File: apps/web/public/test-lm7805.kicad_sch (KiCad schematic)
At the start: 5 parts, among them J1 VIN_CONN, J2 VOUT_5V, U1 LM7805

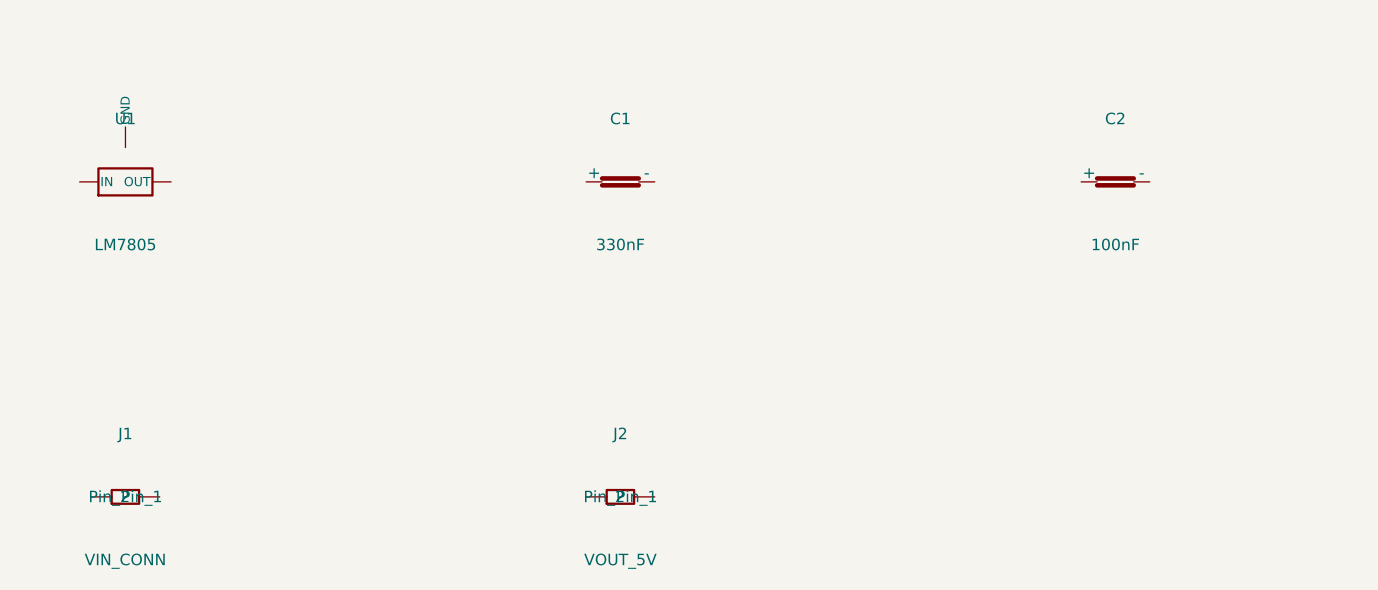
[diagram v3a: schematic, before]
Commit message: fix(schematic): add 20mm side margin to clear inner frame border
Components U1/J1 (left column) and far-right components were drawn
on top of the KiCad inner frame vertical borders (at x=10mm from
paper edge). The previous 12mm margin_side only gave 2mm clearance.

Changes:
- margin_side 12 -> 20mm in _build_flat_schematic_with_net_labels()
  (gives 10mm clearance from inner frame on both sides)
- Regenerated test-lm7805 / test-ne555 / test-esp32 .kicad_sch via
  /circuit-synth/generate (paper width 149 -> 165mm as a result)
- test-cs.html: ResizeObserver on canvas + window load/resize retries
  to reapply auto-zoom when KiCanvas resets its camera on layout
  changes (fixes title block peeking before click-to-interact)

Verified via Chrome DevTools screenshots on all 3 schematic tabs.
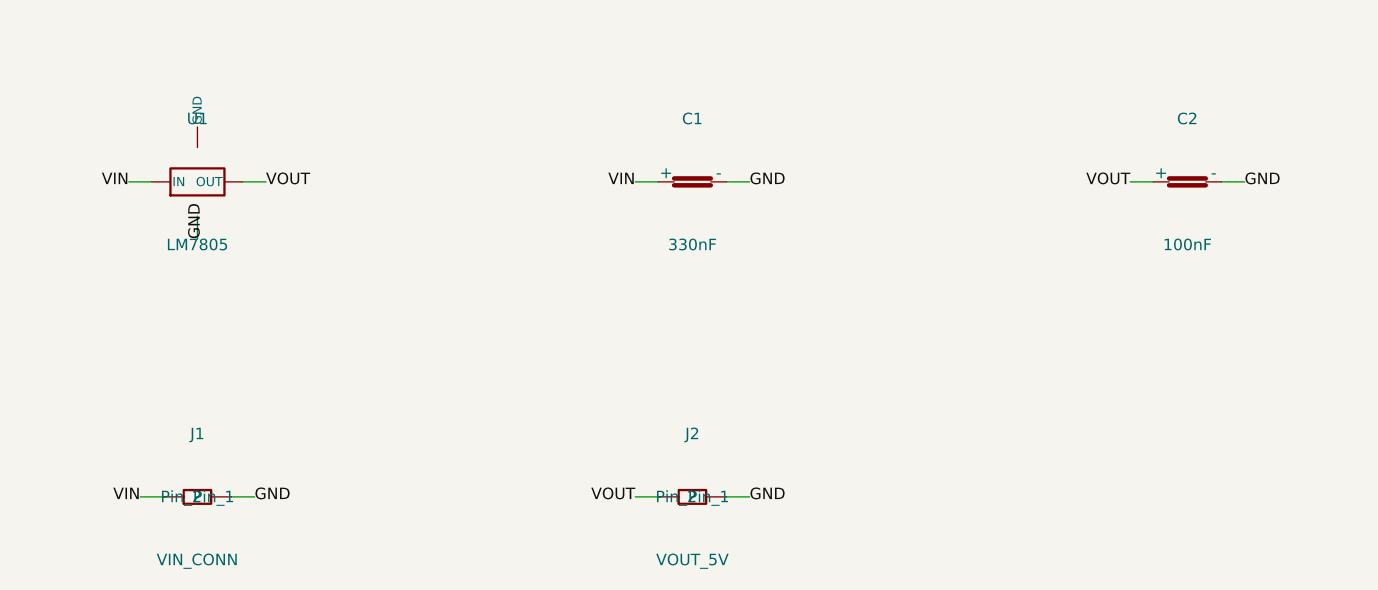
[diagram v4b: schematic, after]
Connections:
- net VIN: now reaches J1.1 (Pin_1)
- net VIN: now also C1.1 (+), U1.1 (IN)
- net GND: now reaches J1.2 (Pin_2)
- net GND: now also C1.2 (-), C2.2 (-), J2.2 (Pin_2)
- net VOUT: now reaches J2.1 (Pin_1)
- net VOUT: now also C2.1 (+), U1.3 (OUT)
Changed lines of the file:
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@@
 (kicad_sch (version 20230121) (generator "layrix-circuit-synth")
-  (paper "User" 149 123)
-  (symbol (lib_id "Device:VReg_3Pin") (at 12 20 0) (unit 1) (in_bom yes) (on_board yes)
-    (property "Reference" "U1" (at 12 13 0) (effects (font (size 1.27 1.27)) (justify center)))
-    (property "Value" "LM7805" (at 12 27 0) (effects (font (size 1.27 1.27)) (justify center)))
-    (property "Footprint" "Package_TO_SOT_THT:TO-220-3_Vertical" (at 12 30 0) (effects (font (size 1.27 1.27)) (hide yes)))
+  (paper "User" 165 123)
+  (symbol (lib_id "Device:VReg_3Pin") (at 20 20 0) (unit 1) (in_bom yes) (on_board yes)
+    (property "Reference" "U1" (at 20 13 0) (effects (font (size 1.27 1.27)) (justify center)))
+    (property "Value" "LM7805" (at 20 27 0) (effects (font (size 1.27 1.27)) (justify center)))
+    (property "Footprint" "Package_TO_SOT_THT:TO-220-3_Vertical" (at 20 30 0) (effects (font (size 1.27 1.27)) (hide yes)))
   )
-  (symbol (lib_id "Device:C") (at 67 20 0) (unit 1) (in_bom yes) (on_board yes)
-    (property "Reference" "C1" (at 67 13 0) (effects (font (size 1.27 1.27)) (justify center)))
-    (property "Value" "330nF" (at 67 27 0) (effects (font (size 1.27 1.27)) (justify center)))
-    (property "Footprint" "Capacitor_THT:C_Disc_D5.0mm_W2.5mm_P5.00mm" (at 67 30 0) (effects (font (size 1.27 1.27)) (hide yes)))
+  (symbol (lib_id "Device:C") (at 75 20 0) (unit 1) (in_bom yes) (on_board yes)
+    (property "Reference" "C1" (at 75 13 0) (effects (font (size 1.27 1.27)) (justify center)))
+    (property "Value" "330nF" (at 75 27 0) (effects (font (size 1.27 1.27)) (justify center)))
+    (property "Footprint" "Capacitor_THT:C_Disc_D5.0mm_W2.5mm_P5.00mm" (at 75 30 0) (effects (font (size 1.27 1.27)) (hide yes)))
   )
-  (symbol (lib_id "Device:C") (at 122 20 0) (unit 1) (in_bom yes) (on_board yes)
-    (property "Reference" "C2" (at 122 13 0) (effects (font (size 1.27 1.27)) (justify center)))
-    (property "Value" "100nF" (at 122 27 0) (effects (font (size 1.27 1.27)) (justify center)))
-    (property "Footprint" "Capacitor_THT:C_Disc_D5.0mm_W2.5mm_P5.00mm" (at 122 30 0) (effects (font (size 1.27 1.27)) (hide yes)))
+  (symbol (lib_id "Device:C") (at 130 20 0) (unit 1) (in_bom yes) (on_board yes)
+    (property "Reference" "C2" (at 130 13 0) (effects (font (size 1.27 1.27)) (justify center)))
+    (property "Value" "100nF" (at 130 27 0) (effects (font (size 1.27 1.27)) (justify center)))
+    (property "Footprint" "Capacitor_THT:C_Disc_D5.0mm_W2.5mm_P5.00mm" (at 130 30 0) (effects (font (size 1.27 1.27)) (hide yes)))
   )
-  (symbol (lib_id "Connector_Generic:Conn_01x02") (at 12 55 0) (unit 1) (in_bom yes) (on_board yes)
-    (property "Reference" "J1" (at 12 48 0) (effects (font (size 1.27 1.27)) (justify center)))
-    (property "Value" "VIN_CONN" (at 12 62 0) (effects (font (size 1.27 1.27)) (justify center)))
-    (property "Footprint" "Connector_PinHeader_2.54mm:PinHeader_1x02_P2.54mm_Vertical" (at 12 65 0) (effects (font (size 1.27 1.27)) (hide yes)))
+  (symbol (lib_id "Connector_Generic:Conn_01x02") (at 20 55 0) (unit 1) (in_bom yes) (on_board yes)
+    (property "Reference" "J1" (at 20 48 0) (effects (font (size 1.27 1.27)) (justify center)))
+    (property "Value" "VIN_CONN" (at 20 62 0) (effects (font (size 1.27 1.27)) (justify center)))
+    (property "Footprint" "Connector_PinHeader_2.54mm:PinHeader_1x02_P2.54mm_Vertical" (at 20 65 0) (effects (font (size 1.27 1.27)) (hide yes)))
   )
-  (symbol (lib_id "Connector_Generic:Conn_01x02") (at 67 55 0) (unit 1) (in_bom yes) (on_board yes)
-    (property "Reference" "J2" (at 67 48 0) (effects (font (size 1.27 1.27)) (justify center)))
-    (property "Value" "VOUT_5V" (at 67 62 0) (effects (font (size 1.27 1.27)) (justify center)))
-    (property "Footprint" "Connector_PinHeader_2.54mm:PinHeader_1x02_P2.54mm_Vertical" (at 67 65 0) (effects (font (size 1.27 1.27)) (hide yes)))
+  (symbol (lib_id "Connector_Generic:Conn_01x02") (at 75 55 0) (unit 1) (in_bom yes) (on_board yes)
+    (property "Reference" "J2" (at 75 48 0) (effects (font (size 1.27 1.27)) (justify center)))
+    (property "Value" "VOUT_5V" (at 75 62 0) (effects (font (size 1.27 1.27)) (justify center)))
+    (property "Footprint" "Connector_PinHeader_2.54mm:PinHeader_1x02_P2.54mm_Vertical" (at 75 65 0) (effects (font (size 1.27 1.27)) (hide yes)))
   )
+  (wire (pts (xy 14.92 20.0) (xy 12.38 20.0)) (stroke (width 0.1524) (type default)))
+  (label "VIN" (at 12.38 20.0 180) (effects (font (size 1.27 1.27))))
+  (wire (pts (xy 71.19 20.0) (xy 68.65 20.0)) (stroke (width 0.1524) (type default)))
+  (label "VIN" (at 68.65 20.0 180) (effects (font (size 1.27 1.27))))
+  (wire (pts (xy 16.19 55.0) (xy 13.65 55.0)) (stroke (width 0.1524) (type default)))
+  (label "VIN" (at 13.65 55.0 180) (effects (font (size 1.27 1.27))))
+  (wire (pts (xy 20.0 23.81) (xy 20.0 26.35)) (stroke (width 0.1524) (type default)))
+  (label "GND" (at 20.0 26.35 90) (effects (font (size 1.27 1.27))))
+  (wire (pts (xy 78.81 20.0) (xy 81.35 20.0)) (stroke (width 0.1524) (type default)))
+  (label "GND" (at 81.35 20.0 0) (effects (font (size 1.27 1.27))))
+  (wire (pts (xy 133.81 20.0) (xy 136.35 20.0)) (stroke (width 0.1524) (type default)))
+  (label "GND" (at 136.35 20.0 0) (effects (font (size 1.27 1.27))))
+  (wire (pts (xy 23.81 55.0) (xy 26.35 55.0)) (stroke (width 0.1524) (type default)))
+  (label "GND" (at 26.35 55.0 0) (effects (font (size 1.27 1.27))))
+  (wire (pts (xy 78.81 55.0) (xy 81.35 55.0)) (stroke (width 0.1524) (type default)))
+  (label "GND" (at 81.35 55.0 0) (effects (font (size 1.27 1.27))))
+  (wire (pts (xy 25.08 20.0) (xy 27.62 20.0)) (stroke (width 0.1524) (type default)))
+  (label "VOUT" (at 27.62 20.0 0) (effects (font (size 1.27 1.27))))
+  (wire (pts (xy 126.19 20.0) (xy 123.65 20.0)) (stroke (width 0.1524) (type default)))
+  (label "VOUT" (at 123.65 20.0 180) (effects (font (size 1.27 1.27))))
+  (wire (pts (xy 71.19 55.0) (xy 68.65 55.0)) (stroke (width 0.1524) (type default)))
+  (label "VOUT" (at 68.65 55.0 180) (effects (font (size 1.27 1.27))))
   (sheet_instances (path "/" (page "1")))
 )

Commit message: fix(schematic): bump margin_side to 28mm so net-label text stays inside frame
Previous 20mm margin put component body 10mm inside the inner frame,
but net-label text ("VIN", "VOUT", "GND"...) extends ~8mm left/right
of the body — so label text sat only ~3mm from the inner frame border,
looking cramped.

New 28mm margin_side accounts for the 8mm label overhang:
  component body at x=28mm
  label text reaches x=28-8=20mm
  inner frame at x=10mm
  -> 10mm visual clearance between label text and frame border

Paper width grows 165 -> 181mm. Regenerated all 3 test schematics.
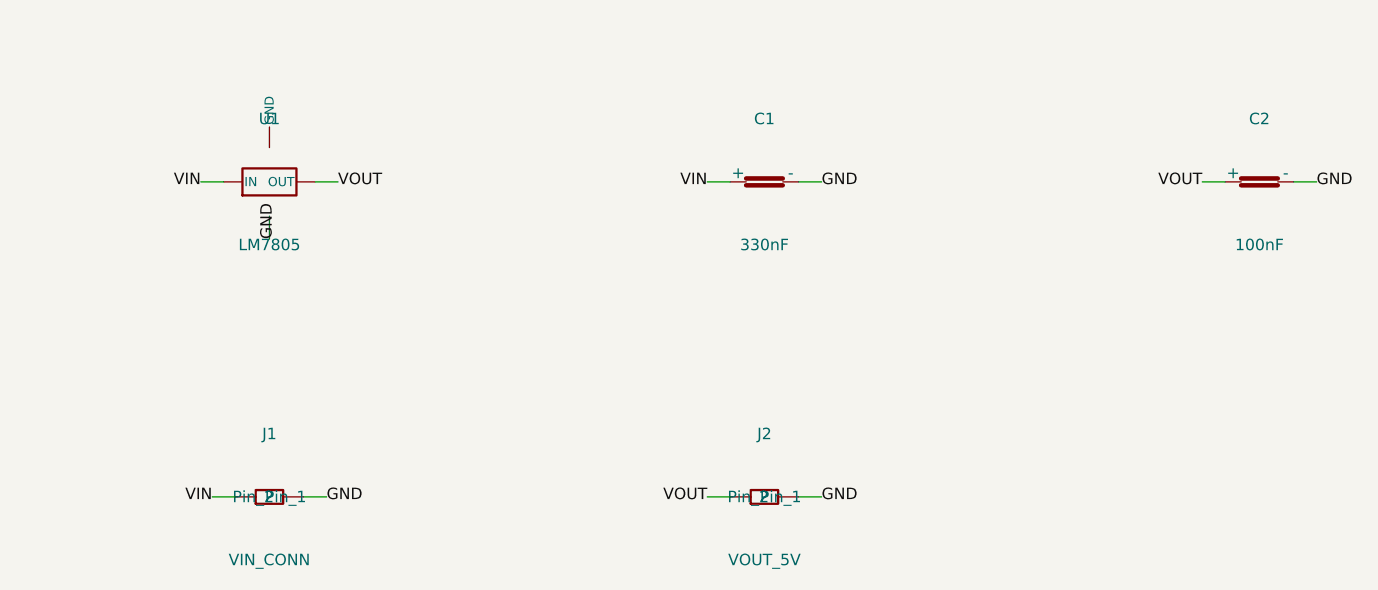
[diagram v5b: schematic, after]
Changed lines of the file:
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@@
 (kicad_sch (version 20230121) (generator "layrix-circuit-synth")
-  (paper "User" 165 123)
-  (symbol (lib_id "Device:VReg_3Pin") (at 20 20 0) (unit 1) (in_bom yes) (on_board yes)
-    (property "Reference" "U1" (at 20 13 0) (effects (font (size 1.27 1.27)) (justify center)))
-    (property "Value" "LM7805" (at 20 27 0) (effects (font (size 1.27 1.27)) (justify center)))
-    (property "Footprint" "Package_TO_SOT_THT:TO-220-3_Vertical" (at 20 30 0) (effects (font (size 1.27 1.27)) (hide yes)))
+  (paper "User" 181 123)
+  (symbol (lib_id "Device:VReg_3Pin") (at 28 20 0) (unit 1) (in_bom yes) (on_board yes)
+    (property "Reference" "U1" (at 28 13 0) (effects (font (size 1.27 1.27)) (justify center)))
+    (property "Value" "LM7805" (at 28 27 0) (effects (font (size 1.27 1.27)) (justify center)))
+    (property "Footprint" "Package_TO_SOT_THT:TO-220-3_Vertical" (at 28 30 0) (effects (font (size 1.27 1.27)) (hide yes)))
   )
-  (symbol (lib_id "Device:C") (at 75 20 0) (unit 1) (in_bom yes) (on_board yes)
-    (property "Reference" "C1" (at 75 13 0) (effects (font (size 1.27 1.27)) (justify center)))
-    (property "Value" "330nF" (at 75 27 0) (effects (font (size 1.27 1.27)) (justify center)))
-    (property "Footprint" "Capacitor_THT:C_Disc_D5.0mm_W2.5mm_P5.00mm" (at 75 30 0) (effects (font (size 1.27 1.27)) (hide yes)))
+  (symbol (lib_id "Device:C") (at 83 20 0) (unit 1) (in_bom yes) (on_board yes)
+    (property "Reference" "C1" (at 83 13 0) (effects (font (size 1.27 1.27)) (justify center)))
+    (property "Value" "330nF" (at 83 27 0) (effects (font (size 1.27 1.27)) (justify center)))
+    (property "Footprint" "Capacitor_THT:C_Disc_D5.0mm_W2.5mm_P5.00mm" (at 83 30 0) (effects (font (size 1.27 1.27)) (hide yes)))
   )
-  (symbol (lib_id "Device:C") (at 130 20 0) (unit 1) (in_bom yes) (on_board yes)
-    (property "Reference" "C2" (at 130 13 0) (effects (font (size 1.27 1.27)) (justify center)))
-    (property "Value" "100nF" (at 130 27 0) (effects (font (size 1.27 1.27)) (justify center)))
-    (property "Footprint" "Capacitor_THT:C_Disc_D5.0mm_W2.5mm_P5.00mm" (at 130 30 0) (effects (font (size 1.27 1.27)) (hide yes)))
+  (symbol (lib_id "Device:C") (at 138 20 0) (unit 1) (in_bom yes) (on_board yes)
+    (property "Reference" "C2" (at 138 13 0) (effects (font (size 1.27 1.27)) (justify center)))
+    (property "Value" "100nF" (at 138 27 0) (effects (font (size 1.27 1.27)) (justify center)))
+    (property "Footprint" "Capacitor_THT:C_Disc_D5.0mm_W2.5mm_P5.00mm" (at 138 30 0) (effects (font (size 1.27 1.27)) (hide yes)))
   )
-  (symbol (lib_id "Connector_Generic:Conn_01x02") (at 20 55 0) (unit 1) (in_bom yes) (on_board yes)
-    (property "Reference" "J1" (at 20 48 0) (effects (font (size 1.27 1.27)) (justify center)))
-    (property "Value" "VIN_CONN" (at 20 62 0) (effects (font (size 1.27 1.27)) (justify center)))
-    (property "Footprint" "Connector_PinHeader_2.54mm:PinHeader_1x02_P2.54mm_Vertical" (at 20 65 0) (effects (font (size 1.27 1.27)) (hide yes)))
+  (symbol (lib_id "Connector_Generic:Conn_01x02") (at 28 55 0) (unit 1) (in_bom yes) (on_board yes)
+    (property "Reference" "J1" (at 28 48 0) (effects (font (size 1.27 1.27)) (justify center)))
+    (property "Value" "VIN_CONN" (at 28 62 0) (effects (font (size 1.27 1.27)) (justify center)))
+    (property "Footprint" "Connector_PinHeader_2.54mm:PinHeader_1x02_P2.54mm_Vertical" (at 28 65 0) (effects (font (size 1.27 1.27)) (hide yes)))
   )
-  (symbol (lib_id "Connector_Generic:Conn_01x02") (at 75 55 0) (unit 1) (in_bom yes) (on_board yes)
-    (property "Reference" "J2" (at 75 48 0) (effects (font (size 1.27 1.27)) (justify center)))
-    (property "Value" "VOUT_5V" (at 75 62 0) (effects (font (size 1.27 1.27)) (justify center)))
-    (property "Footprint" "Connector_PinHeader_2.54mm:PinHeader_1x02_P2.54mm_Vertical" (at 75 65 0) (effects (font (size 1.27 1.27)) (hide yes)))
+  (symbol (lib_id "Connector_Generic:Conn_01x02") (at 83 55 0) (unit 1) (in_bom yes) (on_board yes)
+    (property "Reference" "J2" (at 83 48 0) (effects (font (size 1.27 1.27)) (justify center)))
+    (property "Value" "VOUT_5V" (at 83 62 0) (effects (font (size 1.27 1.27)) (justify center)))
+    (property "Footprint" "Connector_PinHeader_2.54mm:PinHeader_1x02_P2.54mm_Vertical" (at 83 65 0) (effects (font (size 1.27 1.27)) (hide yes)))
   )
-  (wire (pts (xy 14.92 20.0) (xy 12.38 20.0)) (stroke (width 0.1524) (type default)))
-  (label "VIN" (at 12.38 20.0 180) (effects (font (size 1.27 1.27))))
-  (wire (pts (xy 71.19 20.0) (xy 68.65 20.0)) (stroke (width 0.1524) (type default)))
-  (label "VIN" (at 68.65 20.0 180) (effects (font (size 1.27 1.27))))
-  (wire (pts (xy 16.19 55.0) (xy 13.65 55.0)) (stroke (width 0.1524) (type default)))
-  (label "VIN" (at 13.65 55.0 180) (effects (font (size 1.27 1.27))))
-  (wire (pts (xy 20.0 23.81) (xy 20.0 26.35)) (stroke (width 0.1524) (type default)))
-  (label "GND" (at 20.0 26.35 90) (effects (font (size 1.27 1.27))))
-  (wire (pts (xy 78.81 20.0) (xy 81.35 20.0)) (stroke (width 0.1524) (type default)))
-  (label "GND" (at 81.35 20.0 0) (effects (font (size 1.27 1.27))))
-  (wire (pts (xy 133.81 20.0) (xy 136.35 20.0)) (stroke (width 0.1524) (type default)))
-  (label "GND" (at 136.35 20.0 0) (effects (font (size 1.27 1.27))))
-  (wire (pts (xy 23.81 55.0) (xy 26.35 55.0)) (stroke (width 0.1524) (type default)))
-  (label "GND" (at 26.35 55.0 0) (effects (font (size 1.27 1.27))))
-  (wire (pts (xy 78.81 55.0) (xy 81.35 55.0)) (stroke (width 0.1524) (type default)))
-  (label "GND" (at 81.35 55.0 0) (effects (font (size 1.27 1.27))))
-  (wire (pts (xy 25.08 20.0) (xy 27.62 20.0)) (stroke (width 0.1524) (type default)))
-  (label "VOUT" (at 27.62 20.0 0) (effects (font (size 1.27 1.27))))
-  (wire (pts (xy 126.19 20.0) (xy 123.65 20.0)) (stroke (width 0.1524) (type default)))
-  (label "VOUT" (at 123.65 20.0 180) (effects (font (size 1.27 1.27))))
-  (wire (pts (xy 71.19 55.0) (xy 68.65 55.0)) (stroke (width 0.1524) (type default)))
-  (label "VOUT" (at 68.65 55.0 180) (effects (font (size 1.27 1.27))))
+  (wire (pts (xy 22.92 20.0) (xy 20.38 20.0)) (stroke (width 0.1524) (type default)))
+  (label "VIN" (at 20.38 20.0 180) (effects (font (size 1.27 1.27))))
+  (wire (pts (xy 79.19 20.0) (xy 76.65 20.0)) (stroke (width 0.1524) (type default)))
+  (label "VIN" (at 76.65 20.0 180) (effects (font (size 1.27 1.27))))
+  (wire (pts (xy 24.19 55.0) (xy 21.65 55.0)) (stroke (width 0.1524) (type default)))
+  (label "VIN" (at 21.65 55.0 180) (effects (font (size 1.27 1.27))))
+  (wire (pts (xy 28.0 23.81) (xy 28.0 26.35)) (stroke (width 0.1524) (type default)))
+  (label "GND" (at 28.0 26.35 90) (effects (font (size 1.27 1.27))))
+  (wire (pts (xy 86.81 20.0) (xy 89.35 20.0)) (stroke (width 0.1524) (type default)))
+  (label "GND" (at 89.35 20.0 0) (effects (font (size 1.27 1.27))))
+  (wire (pts (xy 141.81 20.0) (xy 144.35 20.0)) (stroke (width 0.1524) (type default)))
+  (label "GND" (at 144.35 20.0 0) (effects (font (size 1.27 1.27))))
+  (wire (pts (xy 31.81 55.0) (xy 34.35 55.0)) (stroke (width 0.1524) (type default)))
+  (label "GND" (at 34.35 55.0 0) (effects (font (size 1.27 1.27))))
+  (wire (pts (xy 86.81 55.0) (xy 89.35 55.0)) (stroke (width 0.1524) (type default)))
+  (label "GND" (at 89.35 55.0 0) (effects (font (size 1.27 1.27))))
+  (wire (pts (xy 33.08 20.0) (xy 35.62 20.0)) (stroke (width 0.1524) (type default)))
+  (label "VOUT" (at 35.62 20.0 0) (effects (font (size 1.27 1.27))))
+  (wire (pts (xy 134.19 20.0) (xy 131.65 20.0)) (stroke (width 0.1524) (type default)))
+  (label "VOUT" (at 131.65 20.0 180) (effects (font (size 1.27 1.27))))
+  (wire (pts (xy 79.19 55.0) (xy 76.65 55.0)) (stroke (width 0.1524) (type default)))
+  (label "VOUT" (at 76.65 55.0 180) (effects (font (size 1.27 1.27))))
   (sheet_instances (path "/" (page "1")))
 )
